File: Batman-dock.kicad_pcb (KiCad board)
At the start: 2 copper layers, 40 x 12 mm, 5 parts, among them J1 TYPECL324LBCP24, J2 70AAJL6LM0G, J3 70AAJL6LM0G

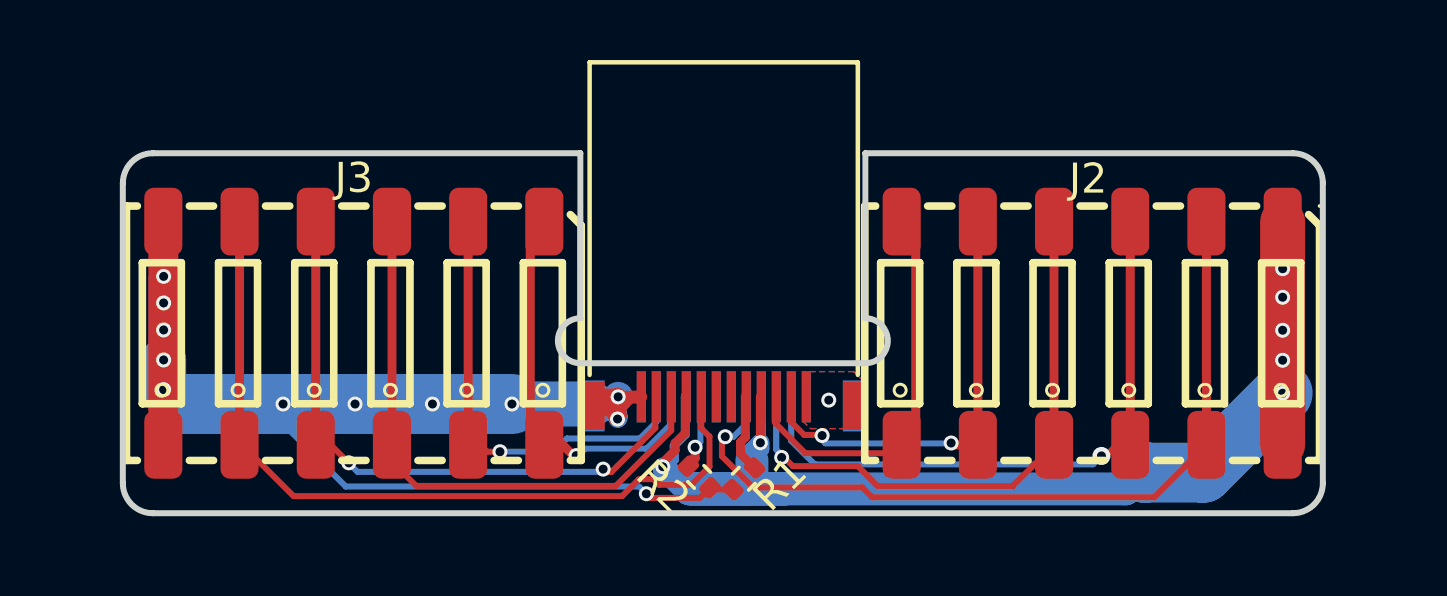
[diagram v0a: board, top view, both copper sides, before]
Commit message: Flipped USB so it's "placed on top"
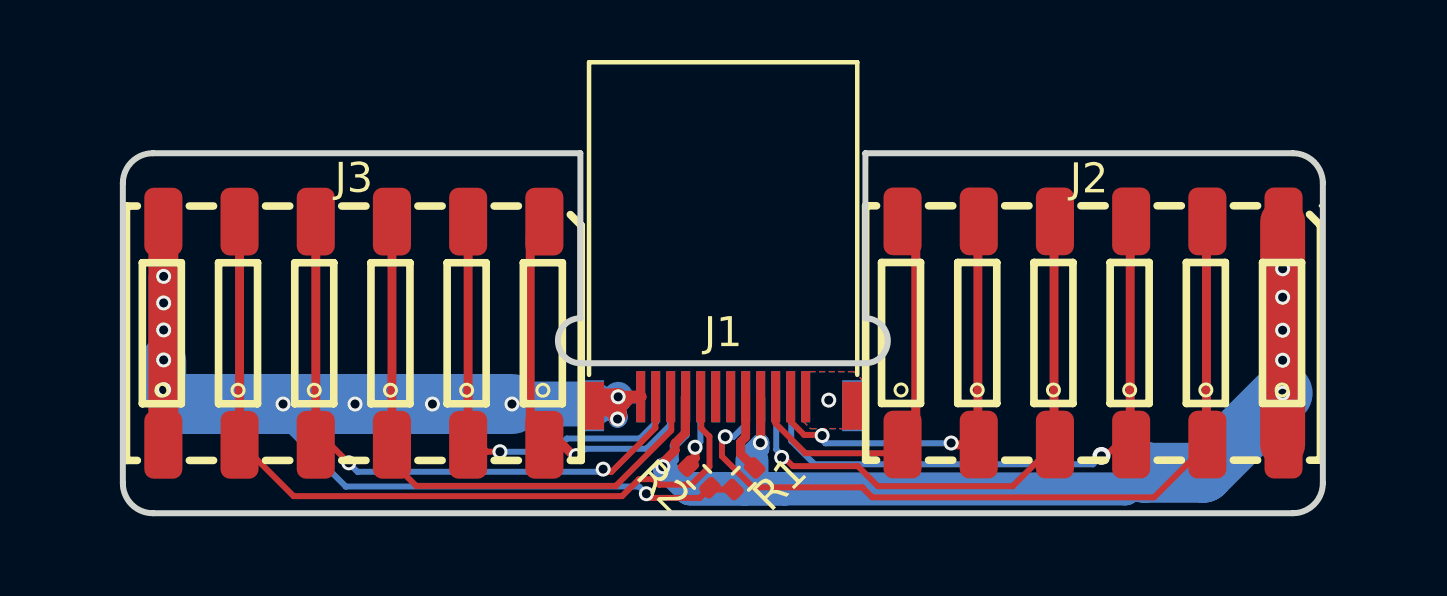
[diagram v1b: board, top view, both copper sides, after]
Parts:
- J1: moved to F.Cu
- moved J1 0.15 mm to (122.2, 96.4), turned to 0 degrees

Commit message: Fixed 70AAJ-6-M0G name
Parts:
- J2, J3: value 70AAJL6LM0G -> 70AAJ-6-M0G

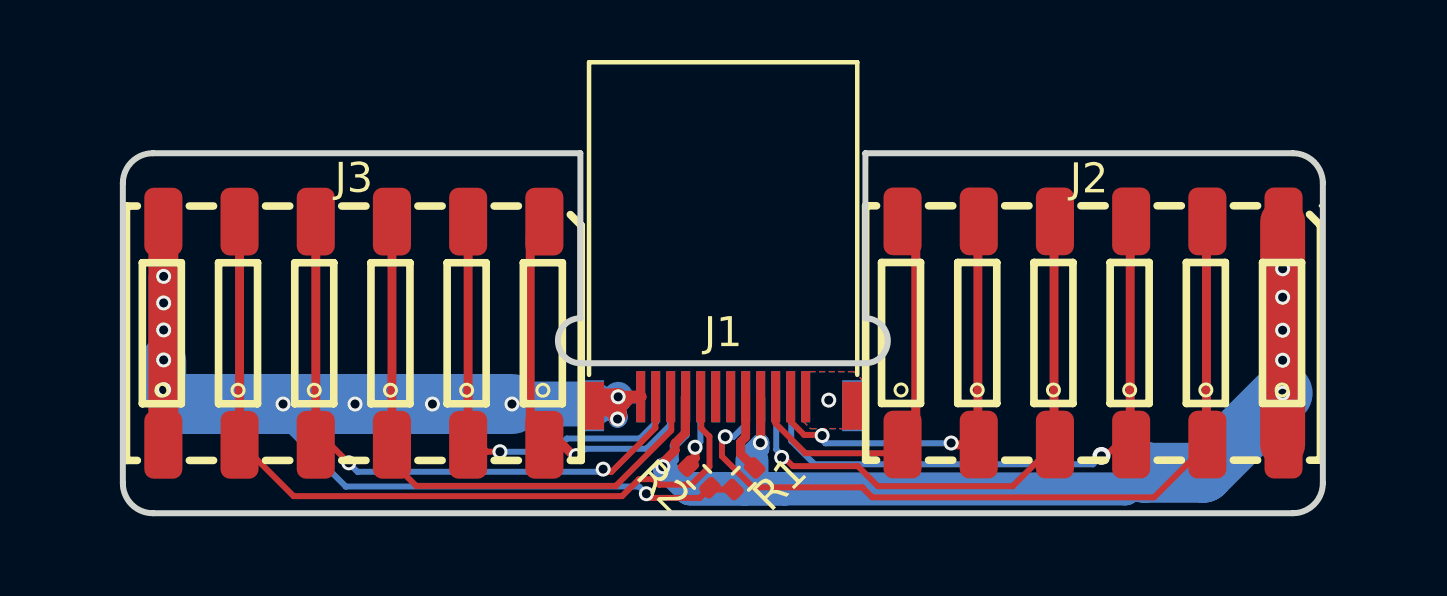
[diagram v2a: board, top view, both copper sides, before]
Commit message: Rev.D added anti-reflection resistors and termination footprints. Added through hole test points
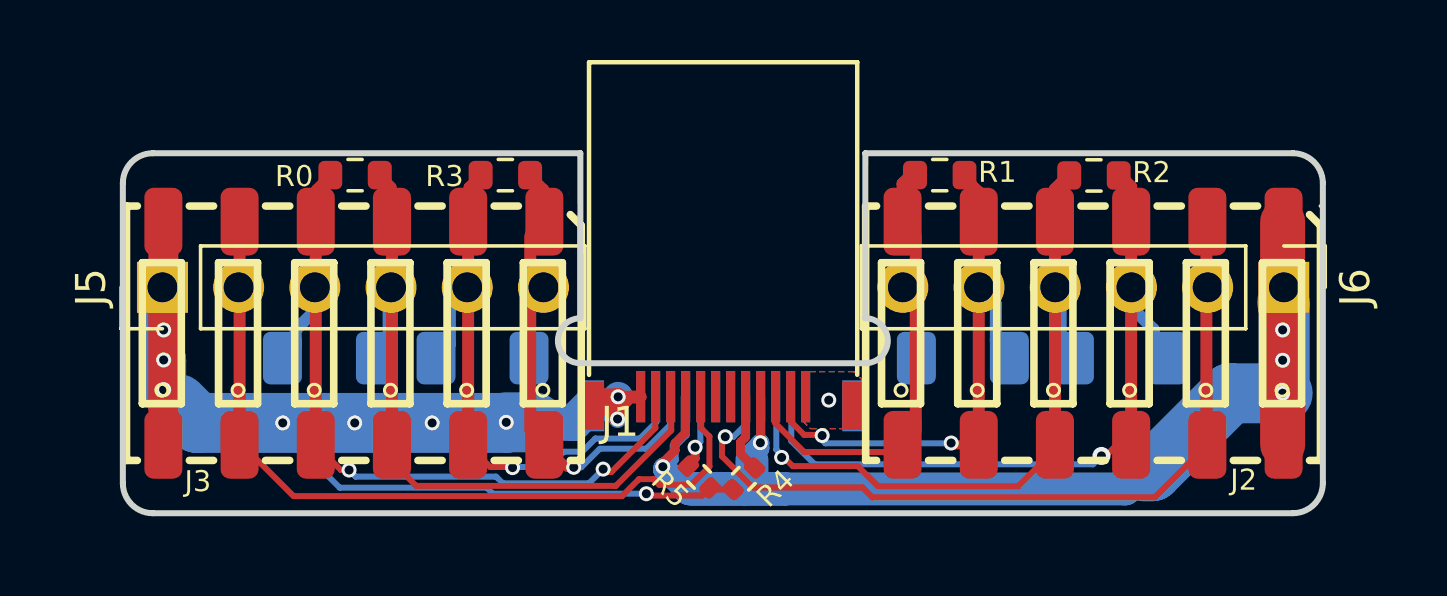
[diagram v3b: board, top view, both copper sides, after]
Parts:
- added CAN0: 120R, Resistor_SMD:R_1206_3216Metric_Pad1.30x1.75mm_HandSolder, B.Cu at (109.1, 95.2)
- added CAN1: 120R, Resistor_SMD:R_1206_3216Metric_Pad1.30x1.75mm_HandSolder, B.Cu at (130.2, 95.2)
- added CAN2: 120R, Resistor_SMD:R_1206_3216Metric_Pad1.30x1.75mm_HandSolder, B.Cu at (135.5, 95.2)
- added CAN3: 120R, Resistor_SMD:R_1206_3216Metric_Pad1.30x1.75mm_HandSolder, B.Cu at (114.2, 95.2)
- added J5: Conn_01x06_Pin, Connector_PinHeader_2.54mm:PinHeader_1x06_P2.54mm_Vertical, F.Cu at (103.5, 92.8)
- added J6: Conn_01x06_Pin, Connector_PinHeader_2.54mm:PinHeader_1x06_P2.54mm_Vertical, F.Cu at (140.9, 92.8)
- added R0: 1k, Resistor_SMD:R_0603_1608Metric, F.Cu at (110.0, 89.0)
- added R1: 1k, Resistor_SMD:R_0603_1608Metric, F.Cu at (129.5, 89.0)
- added R2: 1k, Resistor_SMD:R_0603_1608Metric, F.Cu at (134.6, 89.1)
- added R3: 1k, Resistor_SMD:R_0603_1608Metric, F.Cu at (115.0, 89.0)
- renumbered R1 to R4, R2 to R5
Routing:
- net CAN3_H: track 15.1 -> 20.1 mm
- net CAN0_H: track 20.0 -> 24.9 mm
- net CAN3_L: track 13.5 -> 18.2 mm
- net CAN2_H: track 21.0 -> 25.6 mm
- net CAN1_H: track 14.9 -> 19.5 mm
- net CAN2_L: track 19.6 -> 24.1 mm
- net CAN1_L: track 13.1 -> 17.5 mm
- net CAN0_L: track 19.5 -> 23.9 mm
- net VBUS: track 47.9 -> 46.7 mm, vias 7 -> 5
- net GND: track 50.0 -> 49.4 mm, vias 13 -> 11
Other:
- board text added: "Batman-dock Rev. ${REVISION}"
- board text added: "Vi s2 2H 2L 1H 1L 3L 3H 0L 0H s1 Gn"
- board text removed: "Rev. ${REVISION} Batman-dock"

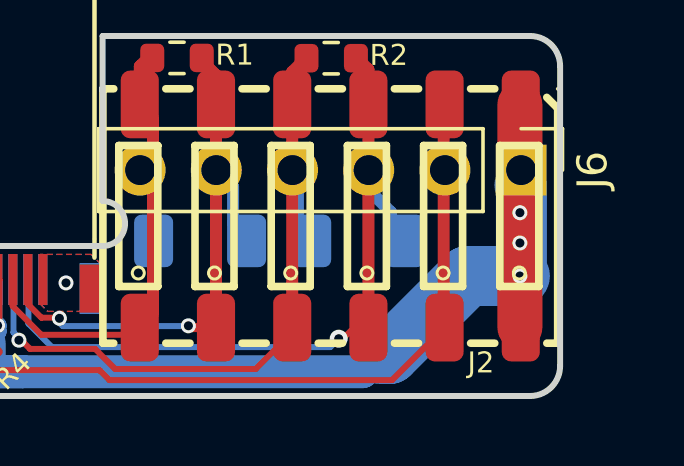
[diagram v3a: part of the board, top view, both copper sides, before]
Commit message: PCB remarks and DNP
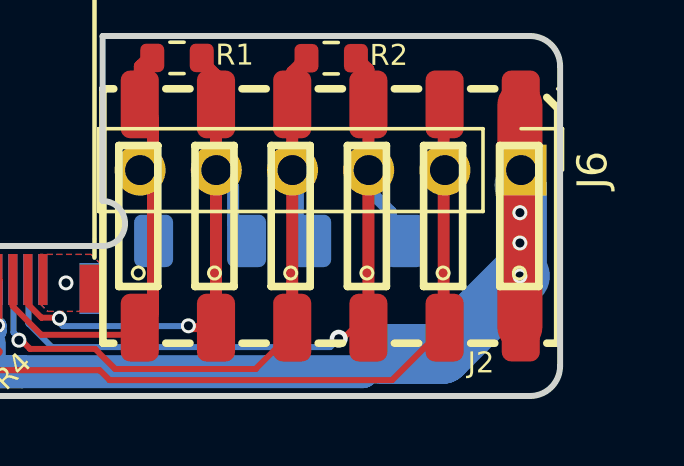
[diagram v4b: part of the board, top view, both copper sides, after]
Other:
- board text added: "1mm PCB thickness Panel spacing >6mm"
